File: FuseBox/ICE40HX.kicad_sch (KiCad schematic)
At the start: 0 parts

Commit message: added ICE40HX
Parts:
- added C16, C17, C18, C19, C22, C23, C24, C25, C26, C27, C28, C29, C30, C31, C32, C33: 100p, symbol Device:C
- added C20, C34: 100n, symbol Device:C
- added C21, C35: 10u, symbol Device:C
- added R18, R21, R22, R23: 1, symbol Device:R
- added R19, R24: 100, symbol Device:R
- added R20: 10k, symbol Device:R
- added TP12, TP13, TP14, TP15, TP16, TP17, TP18, TP19, TP20, TP21, TP22, TP23: TestPoint, symbol Connector:TestPoint
- added U4: ICE40HX8KCT256, Custom:ICE40HX8KCT256, symbol Custom:ICE40HX8KCT256
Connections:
- new net: R20.1, U4.N14 (TRST)
- new net: C20.1, C21.1, R19.1, TP15.1, U4.E8 (VCCPLL1)
- new net: C20.2, C21.2, U4.E7 (GNDPLL1)
- new net: C34.1, C35.1, R24.1, TP22.1, U4.N8 (GNDPLL0)
- new net: C34.2, C35.2, U4.L8 (VCCPLL0)
- new net +1V2: R19.2, R24.2, TP14.1, TP23.1
- new net +3V3: R18.2, R21.2, R22.2, R23.2, TP12.1, TP16.1, TP18.1, TP20.1
- new net FPGA_B1_110: U4.R15 (IOR_110)
- new net FPGA_B1_112: U4.P15 (IOR_112)
- new net GND: C16.2, C17.2, C18.2, C19.2, C22.2, C23.2, C24.2, C25.2, C26.2, C27.2, C28.2, C29.2, C30.2, C31.2, C32.2, C33.2, R20.2
- new net VCCIO0: C16.1, C17.1, C18.1, C19.1, R18.1, TP13.1, U4.A13 (VCCIO_0), U4.A3 (VCCIO_0), U4.A8 (VCCIO_0), U4.F8 (VCCIO_0)
- new net VCCIO1: C22.1, C23.1, C24.1, C25.1, R21.1, TP17.1, U4.C15 (VCCIO_1), U4.H10 (VCCIO_1), U4.H15 (VCCIO_1), U4.N15 (VCCIO_1)
- new net VCCIO2: C26.1, C27.1, C28.1, C29.1, R22.1, TP19.1, U4.K8 (VCCIO_2), U4.P3 (VCCIO_2), U4.R13 (VCCIO_2), U4.R8 (VCCIO_2)
- new net VCCIO3: C30.1, C31.1, C32.1, C33.1, R23.1, TP21.1, U4.E1 (VCCIO_3), U4.G6 (VCCIO_3), U4.J6 (VCCIO_3), U4.N1 (VCCIO_3)
- no-connect marks 0 -> 2
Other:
- note added: "ICE40HX Bank 0"
- note added: "ICE40HX Bank 1"
- note added: "ICE40HX Bank 2"
- note added: "ICE40HX Bank 3"

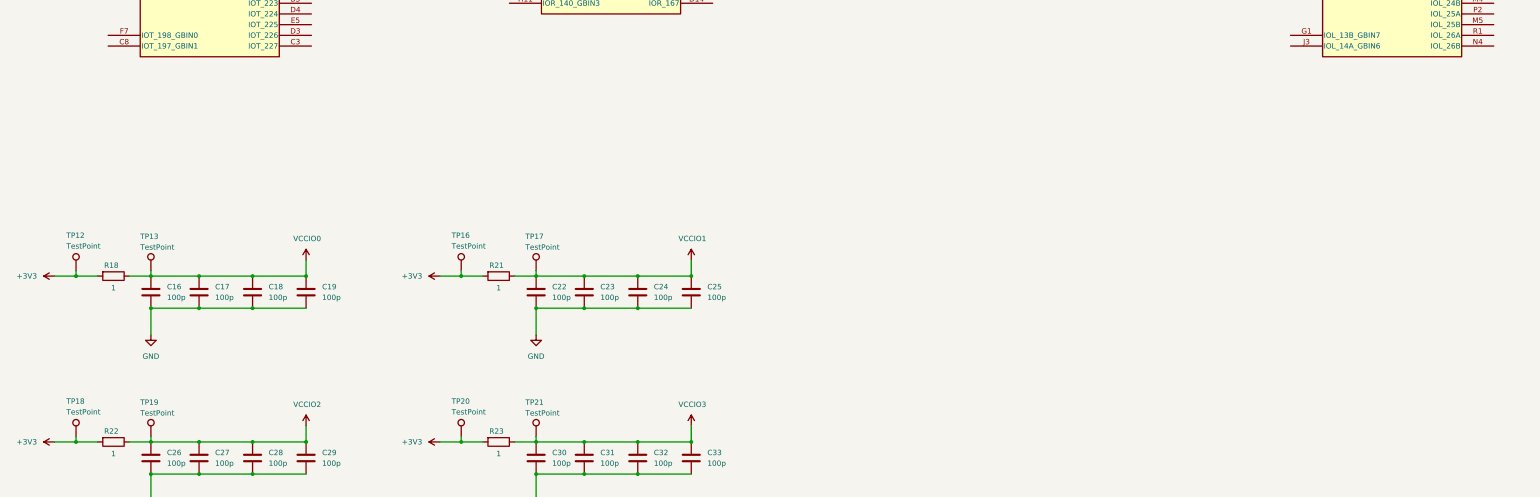
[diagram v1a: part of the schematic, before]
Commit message: added temp USB controllers
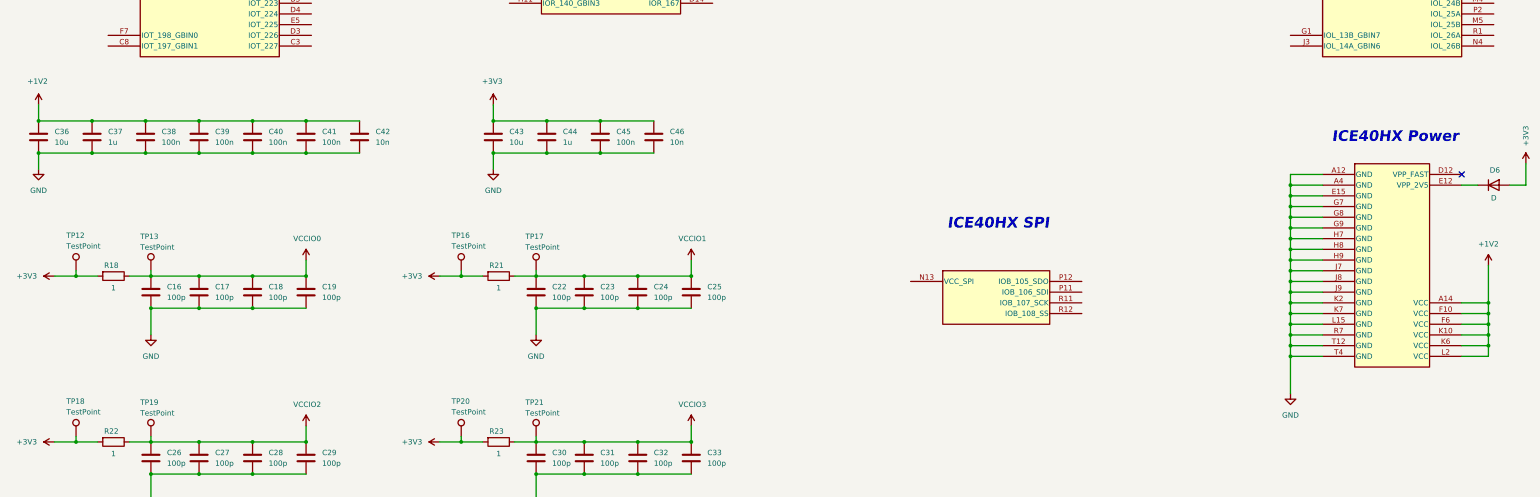
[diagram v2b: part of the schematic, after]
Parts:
- added C36, C43: 10u, symbol Device:C
- added C37, C44: 1u, symbol Device:C
- added C38, C39, C40, C41, C45: 100n, symbol Device:C
- added C42, C46: 10n, symbol Device:C
- added D6: D, symbol Device:D
- added unit 1 of U4
- added unit 6 of U4
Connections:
- net +1V2: now also C36.1, C37.1, C38.1, C39.1, C40.1, C41.1, C42.1, U4.A14 (VCC), U4.F10 (VCC), U4.F6 (VCC), U4.K10 (VCC), U4.K6 (VCC), U4.L2 (VCC)
- net +3V3: now also C43.1, C44.1, C45.1, C46.1, D6.2 (A)
- net GND: now also C36.2, C37.2, C38.2, C39.2, C40.2, C41.2, C42.2, C43.2, C44.2, C45.2, C46.2, U4.A12 (GND), U4.A4 (GND), U4.E15 (GND), U4.G7 (GND), U4.G8 (GND), U4.G9 (GND), U4.H7 (GND), U4.H8 (GND), U4.H9 (GND), U4.J7 (GND), U4.J8 (GND), U4.J9 (GND), U4.K2 (GND), U4.K7 (GND), U4.L15 (GND), U4.R7 (GND), U4.T12 (GND), U4.T4 (GND)
- new net: D6.1 (K), U4.E12 (VPP_2V5)
- no-connect marks 2 -> 3
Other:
- note added: "ICE40HX Power"
- note added: "ICE40HX SPI"

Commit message: changes
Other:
- note added: "Bank 0"
- note added: "Bank 1"
- note added: "Bank 2"
- note added: "Bank 3"
- note removed: "ICE40HX Bank 0"
- note removed: "ICE40HX Bank 1"
- note removed: "ICE40HX Bank 2"
- note removed: "ICE40HX Bank 3"
- note removed: "ICE40HX Power"
- note removed: "ICE40HX SPI"
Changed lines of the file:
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@@
 	(generator_version "9.0")
 	(paper "A3")
-	(text "ICE40HX Bank 1"
+	(text "Bank 1"
 		(exclude_from_sim no)
 		(at 166.878 24.384 0)
@@
 		)
 	)
-	(text "ICE40HX Bank 2"
+	(text "Bank 2"
 		(exclude_from_sim no)
 		(at 261.874 24.384 0)
@@
 		)
 	)
-	(text "ICE40HX Bank 3"
+	(text "Bank 3"
 		(exclude_from_sim no)
 		(at 352.044 23.876 0)
@@
 		)
 	)
-	(text "ICE40HX SPI"
-		(exclude_from_sim no)
-		(at 258.318 200.914 0)
-		(effects
-			(font
-				(size 2.54 2.54)
-				(thickness 0.508)
-				(bold yes)
-				(italic yes)
-			)
-		)
-	)
-	(text "ICE40HX Bank 0"
+	(text "Bank 0"
 		(exclude_from_sim no)
 		(at 71.628 24.13 0)
@@
 		)
 	)
-	(text "ICE40HX Power"
-		(exclude_from_sim no)
-		(at 352.552 180.34 0)
-		(effects
-			(font
-				(size 2.54 2.54)
-				(thickness 0.508)
-				(bold yes)
-				(italic yes)
-			)
-		)
-	)
 	(junction
 		(at 224.79 96.52)
@@
 		(on_board yes)
 		(dnp no)
-		(fields_autoplaced yes)
 		(property "Reference" "#PWR046"
 			(at 34.29 99.06 0)
@@
 		)
 		(property "Value" "+1V2"
-			(at 34.2899 106.68 90)
+			(at 36.322 108.204 0)
 			(effects
 				(font
@@
 		(on_board yes)
 		(dnp no)
-		(fields_autoplaced yes)
 		(property "Reference" "#PWR060"
 			(at 224.79 99.06 0)
@@
 		)
 		(property "Value" "+1V2"
-			(at 224.7899 106.68 90)
+			(at 226.568 107.442 0)
 			(effects
 				(font
@@
 		)
 		(property "Value" "+3V3"
-			(at 383.54 180.086 90)
+			(at 383.286 181.356 0)
 			(effects
 				(font

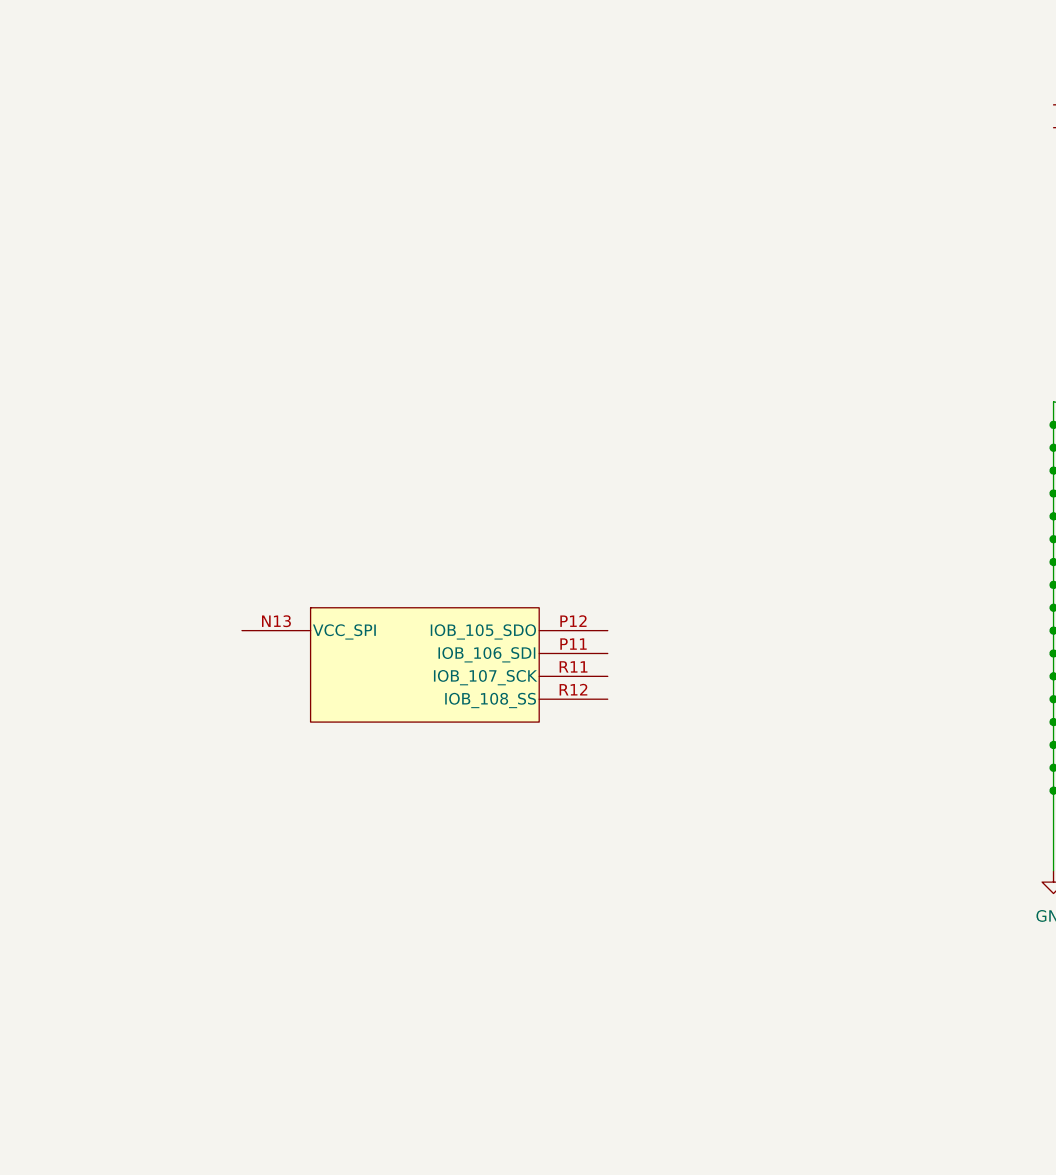
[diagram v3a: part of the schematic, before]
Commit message: added molex terminals
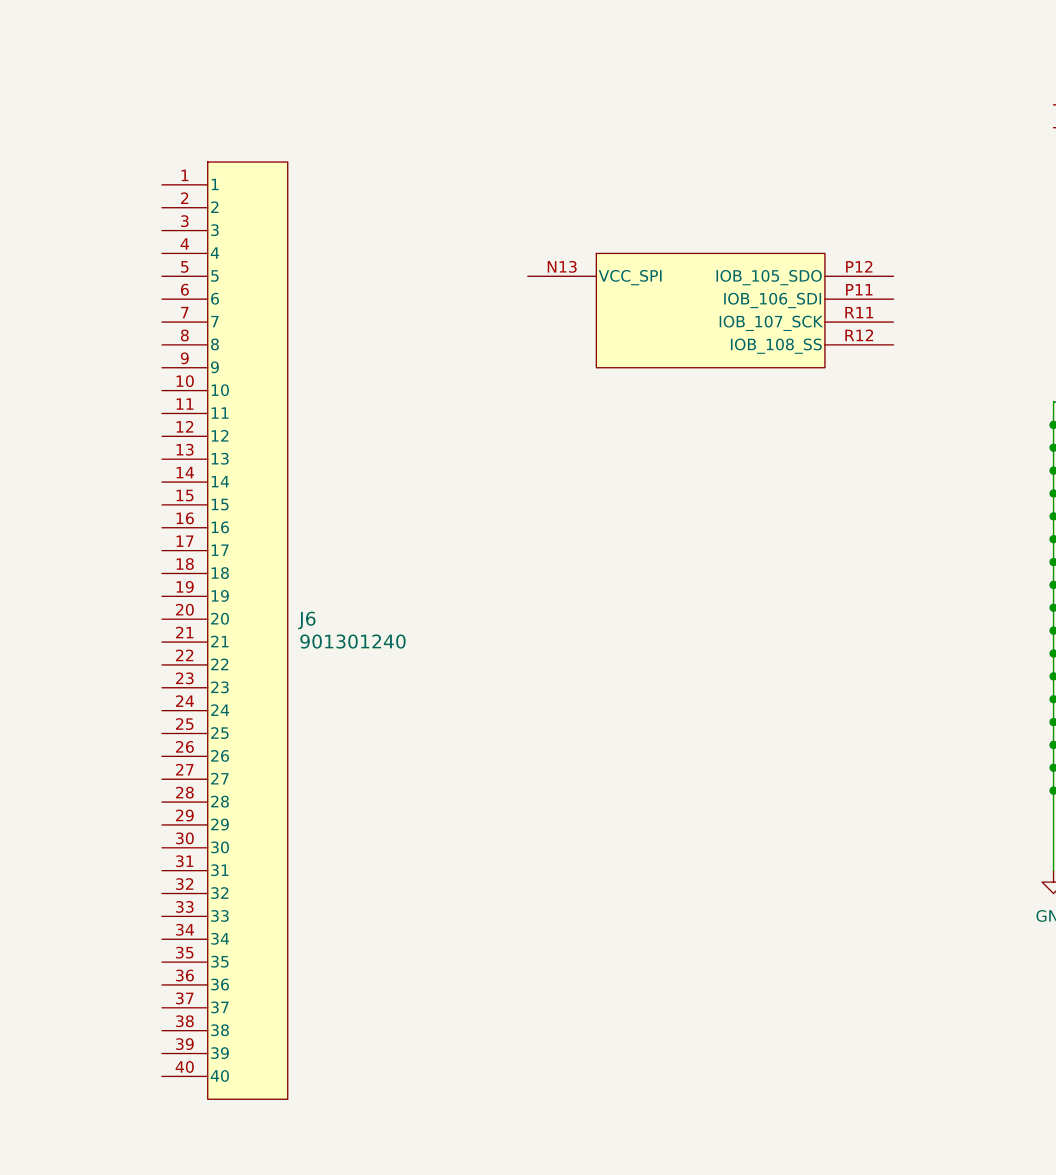
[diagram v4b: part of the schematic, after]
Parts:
- added J6: 901301240, Custom:901301240, symbol Custom:901301240
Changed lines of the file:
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@@
+	)
+	(symbol
+		(lib_id "Custom:901301240")
+		(at 233.68 162.56 0)
+		(unit 1)
+		(exclude_from_sim no)
+		(in_bom yes)
+		(on_board yes)
+		(dnp no)
+		(fields_autoplaced yes)
+		(property "Reference" "J6"
+			(at 243.84 213.3599 0)
+			(effects
+				(font
+					(size 1.524 1.524)
+				)
+				(justify left)
+			)
+		)
+		(property "Value" "901301240"
+			(at 243.84 215.8999 0)
+			(effects
+				(font
+					(size 1.524 1.524)
+				)
+				(justify left)
+			)
+		)
+		(property "Footprint" "Custom:901301240"
+			(at 233.68 152.4 0)
+			(effects
+				(font
+					(size 1.27 1.27)
+					(italic yes)
+				)
+				(hide yes)
+			)
+		)
+		(property "Datasheet" "https://www.molex.com/en-us/products/part-detail-pdf/901301240?display=pdf"
+			(at 234.188 155.448 0)
+			(effects
+				(font
+					(size 1.27 1.27)
+					(italic yes)
+				)
+				(hide yes)
+			)
+		)
+		(property "Description" ""
+			(at 233.68 162.56 0)
+			(effects
+				(font
+					(size 1.27 1.27)
+				)
+				(hide yes)
+			)
+		)
+		(pin "10"
+		)
+		(pin "22"
+		)
+		(pin "2"
+		)
+		(pin "4"
+		)
+		(pin "26"
+		)
+		(pin "28"
+		)
+		(pin "30"
+		)
+		(pin "32"
+		)
+		(pin "1"
+		)
+		(pin "8"
+		)
+		(pin "11"
+		)
+		(pin "12"
+		)
+		(pin "15"
+		)
+		(pin "17"
+		)
+		(pin "3"
+		)
+		(pin "14"
+		)
+		(pin "18"
+		)
+		(pin "20"
+		)
+		(pin "5"
+		)
+		(pin "13"
+		)
+		(pin "19"
+		)
+		(pin "9"
+		)
+		(pin "6"
+		)
+		(pin "16"
+		)
+		(pin "7"
+		)
+		(pin "21"
+		)
+		(pin "23"
+		)
+		(pin "24"
+		)
+		(pin "25"
+		)
+		(pin "27"
+		)
+		(pin "29"
+		)
+		(pin "31"
+		)
+		(pin "38"
+		)
+		(pin "36"
+		)
+		(pin "40"
+		)
+		(pin "35"
+		)
+		(pin "34"
+		)
+		(pin "37"
+		)
+		(pin "39"
+		)
+		(pin "33"
+		)
+		(instances
+			(project ""
+				(path "/7cec0856-4a31-46c4-b6e3-cba19fcff38c/b4e578af-3d50-44df-93ee-873a8251bc3d"
+					(reference "J6")
+					(unit 1)
+				)
+			)
+		)
 	)
 	(symbol
@@
 	(symbol
 		(lib_id "Custom:ICE40HX8KCT256")
-		(at 245.11 212.09 0)
+		(at 276.86 172.72 0)
 		(unit 6)
 		(exclude_from_sim no)
@@
 		(fields_autoplaced yes)
 		(property "Reference" "U4"
-			(at 246.634 210.312 0)
+			(at 278.384 170.942 0)
 			(effects
 				(font
@@
 		)
 		(property "Value" "ICE40HX8KCT256"
-			(at 261.874 203.454 0)
+			(at 293.624 164.084 0)
 			(effects
 				(font
@@
 		)
 		(property "Footprint" "Custom:ICE40HX8KCT256"
-			(at 261.874 209.296 0)
+			(at 293.624 169.926 0)
 			(effects
 				(font
@@
 		)
 		(property "Datasheet" "ICE40HX8K-CT256"
-			(at 261.874 206.502 0)
+			(at 293.624 167.132 0)
 			(effects
 				(font
@@
 		)
 		(property "Description" ""
-			(at 245.11 212.09 0)
-			(effects
-				(font
+			(at 276.86 172.72 0)
+			(effects
+				(font

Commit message: changes
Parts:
- removed J6: 901301240, Custom:901301240, symbol Custom:901301240
- added J10, J11, J6, J9: 901301150, Custom:901301150, symbol Custom:901301150
- added J8: 61301611121, Custom:61301611121, symbol Custom:61301611121
- added R25: 10k, symbol Device:R
- added R26: 649, symbol Device:R
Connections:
- net GND: now also J8.16
- net VCCIO2: now also R25.2, R26.1
- net at U4.B16 (IOR_165): now also J9.44
- net at U4.C16 (IOR_161): now also J9.42
- net at U4.D14 (IOR_167): now also J9.46
- net at U4.D15 (IOR_157): now also J9.39
- net at U4.D16 (IOR_153): now also J9.35
- net at U4.E13 (IOR_166): now also J9.45
- net at U4.E14 (IOR_160): now also J9.41
- net at U4.E16 (IOR_151): now also J9.33
- net at U4.F11 (IOR_158): now also J9.40
- net at U4.F12 (IOR_156): now also J9.38
- net at U4.F13 (IOR_162): now also J9.43
- net at U4.F14 (IOR_155): now also J9.37
- net at U4.F15 (IOR_149): now also J9.31
- net at U4.F16 (IOR_147): now also J9.29
- net at U4.G10 (IOR_146): now also J9.28
- net at U4.G11 (IOR_148): now also J9.30
- net at U4.G12 (IOR_154): now also J9.36
- net at U4.G13 (IOR_152): now also J9.34
- net at U4.G14 (IOR_150): now also J9.32
- net at U4.G15 (IOR_145): now also J9.27
- net at U4.G16 (IOR_143): now also J9.25
- net at U4.H12 (IOR_144): now also J9.26
- net at U4.H13 (IOR_139): now also J9.23
- net at U4.H14 (IOR_142): now also J9.24
- net at U4.J10 (IOR_122): now also J9.10
- net at U4.J11 (IOR_126): now also J9.12
- net at U4.J12 (IOR_136): now also J9.20
- net at U4.J13 (IOR_137): now also J9.21
- net at U4.J14 (IOR_134): now also J9.19
- net at U4.J15 (IOR_130): now also J9.16
- net at U4.J16 (IOR_138): now also J9.22
- net at U4.K12 (IOR_120): now also J9.8
- net at U4.K13 (IOR_128): now also J9.14
- net at U4.K14 (IOR_129): now also J9.15
- net at U4.K15 (IOR_131): now also J9.17
- net at U4.K16 (IOR_133): now also J9.18
- net at U4.L12 (IOR_116): now also J9.4
- net at U4.L13 (IOR_118): now also J9.6
- net at U4.L14 (IOR_119): now also J9.7
- net at U4.L16 (IOR_127): now also J9.13
- net at U4.M13 (IOR_114): now also J9.2
- net at U4.M14 (IOR_115): now also J9.3
- net at U4.M15 (IOR_123): now also J9.11
- net at U4.M16 (IOR_121): now also J9.9
- net ICE_JTAG_TRST: now reaches R20.1, U4.N14 (TRST)
- net ICE_JTAG_TRST: now also J8.6
- net at U4.N16 (IOR_117): now also J9.5
- net at U4.P16 (IOR_113): now also J9.1
- net at U4.A1 (IOT_220): now also J6.43
- net at U4.A10 (IOT_186): now also J6.18
- net at U4.A11 (IOT_187): now also J6.19
- net at U4.A15 (IOT_177): now also J6.9
- net at U4.A16 (IOT_176): now also J6.8
- net at U4.A2 (IOT_218): now also J6.41
- net at U4.A5 (IOT_213): now also J6.37
- net at U4.A6 (IOT_211): now also J6.35
- net at U4.A7 (IOT_205): now also J6.29
- net at U4.A9 (IOT_194): now also J6.24
- net at U4.B10 (IOT_183): now also J6.15
- net at U4.B11 (IOT_184): now also J6.16
- net at U4.B12 (IOT_182): now also J6.14
- net at U4.B13 (IOT_178): now also J6.10
- net at U4.B14 (IOT_171): now also J6.4
- net at U4.B15 (IOT_169): now also J6.2
- net at U4.B3 (IOT_223): now also J6.46
- net at U4.B4 (IOT_216): now also J6.40
- net at U4.B5 (IOT_214): now also J6.38
- net at U4.B6 (IOT_208): now also J6.32
- net at U4.B7 (IOT_207): now also J6.31
- net at U4.B8 (IOT_203): now also J6.28
- net at U4.B9 (IOT_199): now also J6.26
- net at U4.C10 (IOT_185): now also J6.17
- net at U4.C11 (IOT_180): now also J6.12
- net at U4.C12 (IOT_172): now also J6.5
- net at U4.C13 (IOT_174): now also J6.7
- net at U4.C14 (IOT_168): now also J6.1
- net at U4.C3 (IOT_227): now also J6.50
- net at U4.C4 (IOT_222): now also J6.45
- net at U4.C5 (IOT_221): now also J6.44
- net at U4.C6 (IOT_209): now also J6.33
- net at U4.C7 (IOT_206): now also J6.30
- net at U4.C9 (IOT_191): now also J6.21
- net at U4.D10 (IOT_190): now also J6.20
- net at U4.D11 (IOT_181): now also J6.13
- net at U4.D13 (IOT_170): now also J6.3
- net at U4.D3 (IOT_226): now also J6.49
- net at U4.D4 (IOT_224): now also J6.47
- net at U4.D5 (IOT_219): now also J6.42
- net at U4.D6 (IOT_212): now also J6.36
- net at U4.D7 (IOT_210): now also J6.34
- net at U4.D8 (IOT_200): now also J6.27
- net at U4.D9 (IOT_193): now also J6.23
- net at U4.E10 (IOT_179): now also J6.11
- net at U4.E11 (IOT_173): now also J6.6
- net at U4.E5 (IOT_225): now also J6.48
- net at U4.E6 (IOT_215): now also J6.39
- net at U4.E9 (IOT_192): now also J6.22
- net at U4.F9 (IOT_196): now also J6.25
- net at U4.L10 (IOB_85): now also J10.29
- net at U4.L11 (IOB_99): now also J10.39
- net at U4.L9 (IOB_74): now also J10.20
- net ICE_CDONE: now reaches U4.M10 (CDONE)
- net ICE_CDONE: now also J8.8, R26.2
- net at U4.M11 (IOB_93): now also J10.36
- net at U4.M12 (IOB_101): now also J10.41
- net at U4.M7 (IOB_64): now also J10.12
- net at U4.M8 (IOB_68): now also J10.15
- net at U4.M9 (IOB_80): now also J10.26
- net at U4.N10 (IOB_87): now also J10.31
- net ICE_CRESET_B: now reaches U4.N11 (CRESET_B)
- net ICE_CRESET_B: now also J8.9, R25.1
- net at U4.N12 (IOB_98): now also J10.38
- net at U4.N5 (IOB_56): now also J10.5
- net at U4.N6 (IOB_52): now also J10.1
- net at U4.N7 (IOB_66): now also J10.13
- net at U4.N9 (IOB_78): now also J10.24
- net at U4.P10 (IOB_86): now also J10.30
- net at U4.P4 (IOB_54): now also J10.3
- net at U4.P5 (IOB_58): now also J10.7
- net at U4.P6 (IOB_67): now also J10.14
- net at U4.P7 (IOB_77): now also J10.23
- net at U4.P8 (IOB_72): now also J10.18
- net at U4.P9 (IOB_83): now also J10.27
- net at U4.R10 (IOB_84): now also J10.28
- net at U4.R16 (IOB_102): now also J10.42
- net at U4.R2 (IOB_55): now also J10.4
- net at U4.R3 (IOB_59): now also J10.8
- net at U4.R4 (IOB_63): now also J10.11
- net at U4.R5 (IOB_60): now also J10.9
- net at U4.R6 (IOB_71): now also J10.17
- net at U4.T1 (IOB_53): now also J10.2
- net at U4.T10 (IOB_88): now also J10.32
- net at U4.T11 (IOB_89): now also J10.33
- net at U4.T13 (IOB_94): now also J10.37
- net at U4.T14 (IOB_92): now also J10.35
- net at U4.T15 (IOB_91): now also J10.34
- net at U4.T16 (IOB_100): now also J10.40
- net at U4.T2 (IOB_57): now also J10.6
- net at U4.T3 (IOB_61): now also J10.10
- net at U4.T5 (IOB_69): now also J10.16
- net at U4.T6 (IOB_73): now also J10.19
- net at U4.T7 (IOB_75): now also J10.21
- net at U4.T8 (IOB_76): now also J10.22
- net at U4.T9 (IOB_79): now also J10.25
- net at U4.B1 (IOL_2B): now also J11.4
- net at U4.B2 (IOL_1B): now also J11.2
- net at U4.C1 (IOL_3A): now also J11.5
- net at U4.C2 (IOL_3B): now also J11.6
- net at U4.D1 (IOL_5B): now also J11.10
- net at U4.D2 (IOL_4B): now also J11.8
- net at U4.E2 (IOL_7B): now also J11.14
- net at U4.E3 (IOL_6B): now also J11.12
- net at U4.E4 (IOL_1A): now also J11.1
- net at U4.F1 (IOL_10B): now also J11.20
- net at U4.F2 (IOL_9B): now also J11.18
- net at U4.F3 (IOL_8B): now also J11.16
- net at U4.F4 (IOL_4A): now also J11.7
- net at U4.F5 (IOL_2A): now also J11.3
- net at U4.G2 (IOL_11B): now also J11.22
- net at U4.G3 (IOL_8A): now also J11.15
- net at U4.G4 (IOL_6A): now also J11.11
- net at U4.G5 (IOL_5A): now also J11.9
- net at U4.H1 (IOL_14B): now also J11.26
- net at U4.H2 (IOL_12B): now also J11.24
- net at U4.H3 (IOL_9A): now also J11.17
- net at U4.H4 (IOL_11A): now also J11.21
- net at U4.H5 (IOL_7A): now also J11.13
- net at U4.H6 (IOL_10A): now also J11.19
- net at U4.J1 (IOL_15B): now also J11.28
- net at U4.J2 (IOL_15A): now also J11.27
- net at U4.J4 (IOL_12A): now also J11.23
- net at U4.J5 (IOL_13A): now also J11.25
- net at U4.K1 (IOL_16A): now also J11.29
- net at U4.K3 (IOL_16B): now also J11.30
- net at U4.K4 (IOL_18A): now also J11.33
- net at U4.K5 (IOL_20A): now also J11.37
- net at U4.L1 (IOL_17B): now also J11.32
- net at U4.L3 (IOL_19B): now also J11.36
- net at U4.L4 (IOL_17A): now also J11.31
- net at U4.L5 (IOL_23A): now also J11.43
- net at U4.L6 (IOL_19A): now also J11.35
- net at U4.L7 (IOL_21A): now also J11.39
- net at U4.M1 (IOL_18B): now also J11.34
- net at U4.M2 (IOL_20B): now also J11.38
- net at U4.M3 (IOL_22B): now also J11.42
- net at U4.M4 (IOL_24B): now also J11.46
- net at U4.M5 (IOL_25B): now also J11.48
- net at U4.M6 (IOL_22A): now also J11.41
- net at U4.N2 (IOL_21B): now also J11.40
- net at U4.N3 (IOL_23B): now also J11.44
- net at U4.N4 (IOL_26B): now also J11.50
- net at U4.P1 (IOL_24A): now also J11.45
- net at U4.P2 (IOL_25A): now also J11.47
- net at U4.R1 (IOL_26A): now also J11.49
- net ICE_JTAG_VCC: now reaches U4.N13 (VCC_SPI)
- net ICE_JTAG_VCC: now also J8.1
- net ICE_JTAG_SDI: now reaches U4.P11 (IOB_106_SDI)
- net ICE_JTAG_SDI: now also J8.3
- net ICE_JTAG_SDO: now reaches U4.P12 (IOB_105_SDO)
- net ICE_JTAG_SDO: now also J8.2
- net ICE_JTAG_SCK: now reaches U4.R11 (IOB_107_SCK)
- net ICE_JTAG_SCK: now also J8.4
- net ICE_JTAG_SS: now reaches U4.R12 (IOB_108_SS)
- net ICE_JTAG_SS: now also J8.5
- net FPGA_B1_110 renamed ICE_B1_110
- net FPGA_B1_112 renamed ICE_B1_112
- no-connect marks 3 -> 20
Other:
- moved on the sheet: D6, R20
